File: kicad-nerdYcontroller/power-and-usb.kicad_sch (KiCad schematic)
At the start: 3 parts, among them P201 USB_C_Plug_USB2.0, U201 AMS1117-3.3

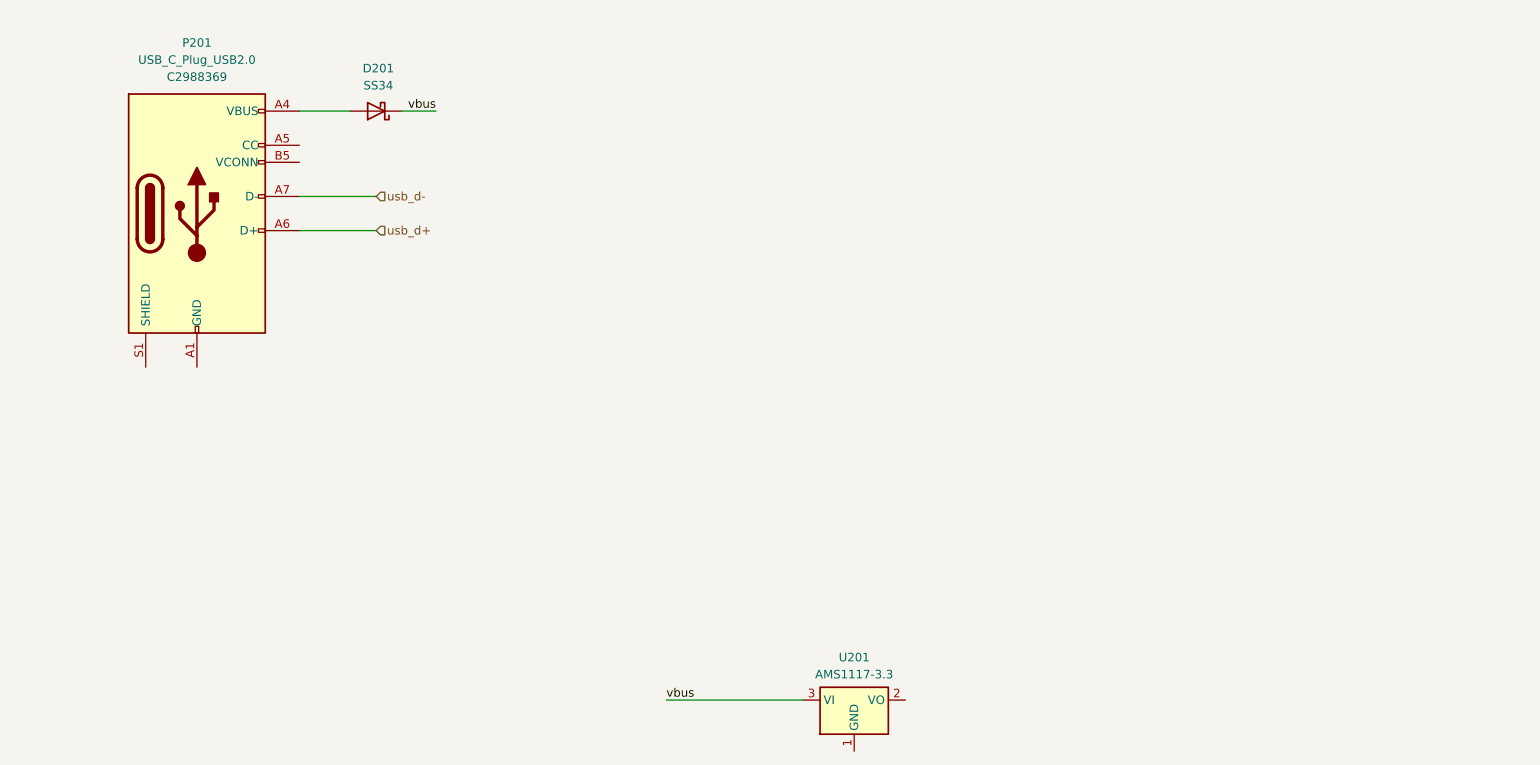
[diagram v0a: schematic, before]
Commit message: Adding components to USB-C and 3V3 LDO
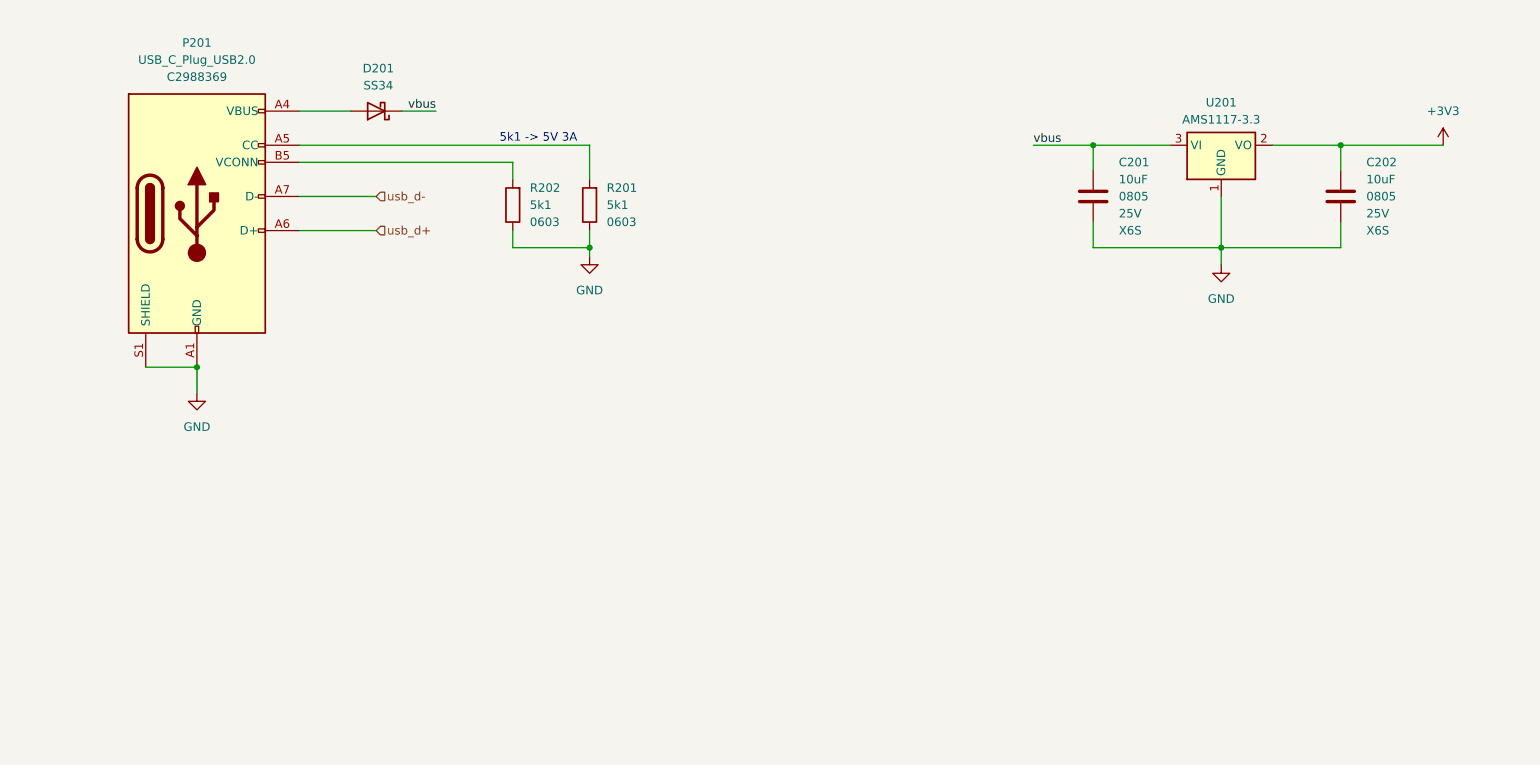
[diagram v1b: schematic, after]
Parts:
- added C201, C202: 10uF, Capacitor_SMD:C_0805_2012Metric, symbol kidslab:C-10uF-0805-25V
- added R201, R202: 5k1, Resistor_SMD:R_0603_1608Metric, symbol kidslab:R-5k1-0603
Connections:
- net vbus: now also C201.1
- net GND: now reaches P201.A1 (GND), P201.A12 (GND), P201.B1 (GND), P201.B12 (GND)
- net GND: now also P201.S1 (SHIELD), U201.1 (GND), C201.2, C202.2, R201.1, R202.1
- net at P201.A5 (CC): now also R201.2
- net at P201.B5 (VCONN): now also R202.2
- net +3V3: now reaches U201.2 (VO)
- net +3V3: now also C202.1
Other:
- note added: "5k1 -> 5V 3A"
- moved on the sheet: U201

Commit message: Adding kicad-nerdYController
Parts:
- added D202: ESD7L5.0DT5G, Package_TO_SOT_SMD:SOT-723, symbol kidslab:ESDA5V3L
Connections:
- net GND: now also D202.3 (A); no longer P201.S1 (SHIELD)
- net usb_d+: now also D202.2 (K)
- net usb_d-: now also D202.1 (K)
- net +3V3 renamed +3V3_out
- net vbus renamed VBUS
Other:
- note added: "3V3 - LDO"
- note added: "Add 100R Add 1nF"

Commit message: Adding KiCad files for first controller production.
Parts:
- removed D201: SS34, Diode_SMD:D_SMA, symbol kidslab:SS34
- removed D202: ESD7L5.0DT5G, Package_TO_SOT_SMD:SOT-723, symbol kidslab:ESDA5V3L
- removed P201: USB_C_Plug_USB2.0, Connector_USB:USB_C_Receptacle_G-Switch_GT-USB-7010ASV, symbol kidslab:USB_C_Plug_USB2.0
- added C203: 1nF, Capacitor_SMD:C_0603_1608Metric, symbol kidslab:C-1nF-0603-50V
- added D201, D203: B5817W, Diode_SMD:D_SOD-123, symbol kidslab: B5817W Schottky Diode
- added D202: PRTR5V0U2F, Package_SON:WSON-6_1.5x1.5mm_P0.5mm, symbol kidslab:PRTR5V0U2F
- added J201: S2B-PH-SM4-TB, kidslab:JST_PH_S2B-PH-SM4-TB_1x02-1MP_P2.00mm_Horizontal, symbol kidslab:Battery Connector JST
- added P201: USB_C_Plug_USB2.0, kidslab:USB_C_Receptacle_GCT_USB4110, symbol kidslab:USB_C_Plug_USB2.0 GCT_USB4110
- added R203: 100, Resistor_SMD:R_0603_1608Metric, symbol kidslab:R-100R-0603
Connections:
- net GND: now also C203.2, D202.2 (GND), J201.2 (Pin_2), P201.A1 (GND), P201.A12 (GND), P201.B1 (GND), P201.B12 (GND), R203.1
- net VBUS: now also D201.1 (K), D203.1 (K)
- net usb_d+: now also D202.6 (IO1)
- net usb_d-: now also D202.4 (IO2)
- net at R202.2: now also P201.B5 (VCONN)
- net at R201.2: now also P201.A5 (CC)
- new net: D203.2 (A), J201.1 (Pin_1)
- new net: C203.1, P201.S1 (SHIELD), R203.2
- new net USBC-D+: D202.1 (IO1), P201.A6 (D+)
- new net USBC-D-: D202.3 (IO2), P201.A7 (D-)
- new net usb_vcc: D201.2 (A), D202.5 (VCC), P201.A4 (VBUS), P201.A9 (VBUS), P201.B4 (VBUS), P201.B9 (VBUS)
- no-connect marks 0 -> 1
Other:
- note removed: "Add 100R Add 1nF"
